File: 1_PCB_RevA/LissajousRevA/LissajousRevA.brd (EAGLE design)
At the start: 100 x 80 mm, 77 parts, among them U101 LM348D, U201 LM348D, U401 LM348D

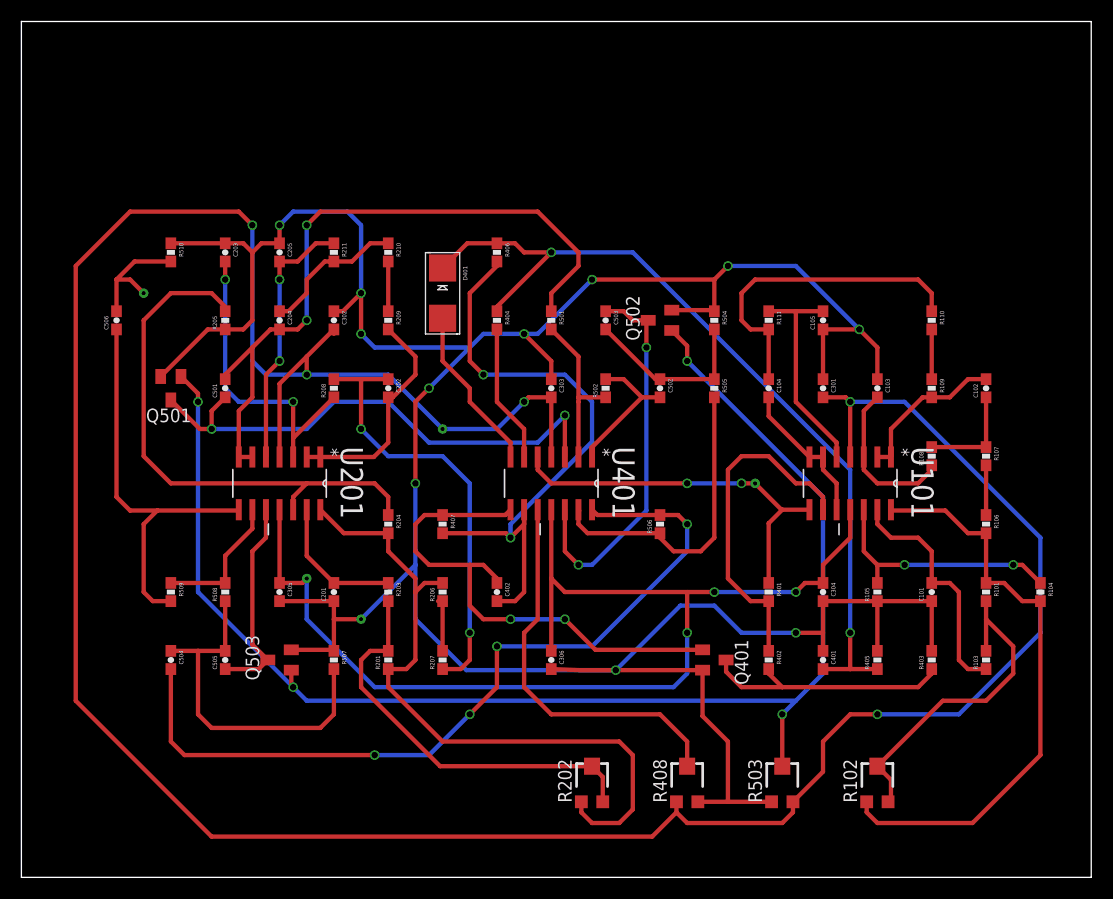
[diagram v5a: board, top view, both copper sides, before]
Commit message: bring test points to bottom of pcb
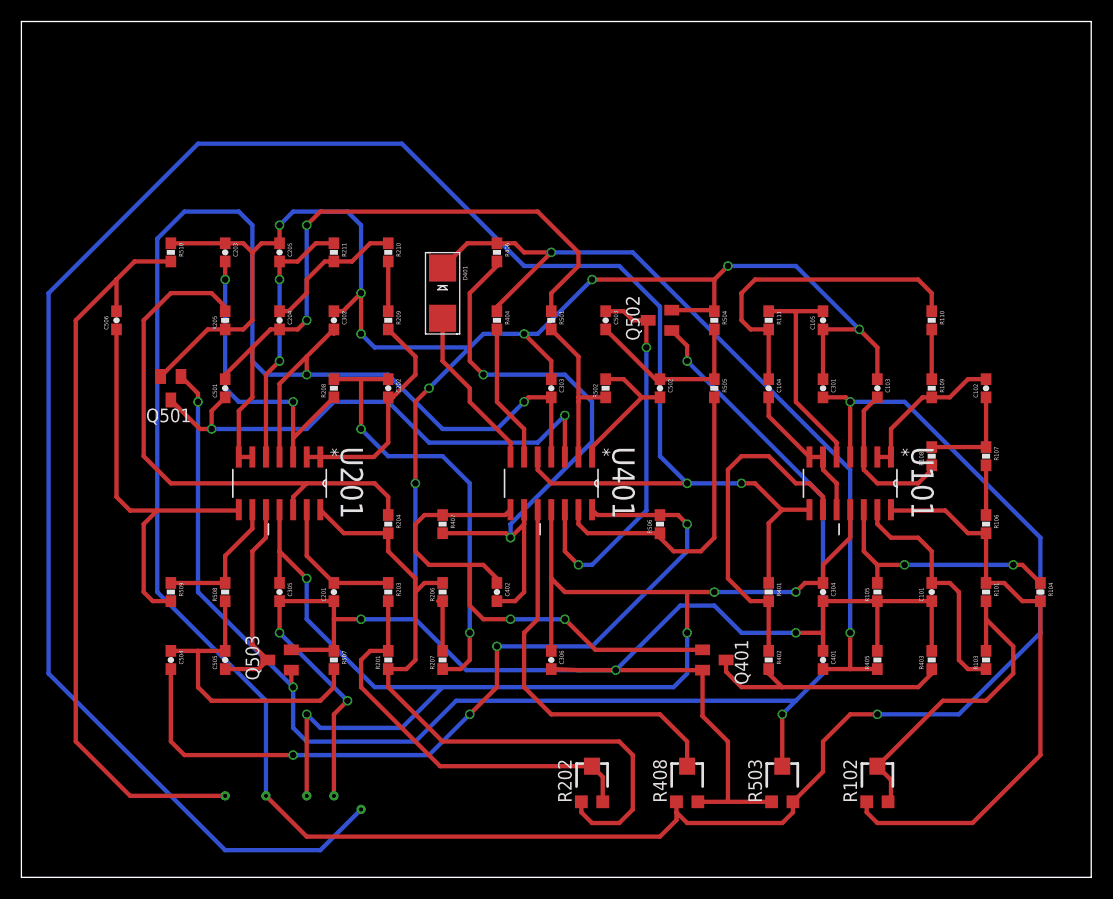
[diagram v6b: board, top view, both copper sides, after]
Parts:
- moved TP304 47.8 mm to (31.8, 6.35)
- moved TP305 47.6 mm to (19.1, 7.62)
- moved TP301 38.1 mm to (22.9, 7.62)
- moved TP302 20.3 mm to (26.7, 7.62)
- moved TP303 16.7 mm to (29.2, 7.62)
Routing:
- net VIEW1: track 35.5 -> 195.5 mm
- net VIEW2: track 11.8 -> 69.6 mm
- net V-: track 107.1 -> 130.4 mm, vias 3 -> 5
- net 0V: track 283.1 -> 302.4 mm, vias 11 -> 14
- net V+: track 273.2 -> 259.1 mm, vias 5 -> 4
- net N$38: track 130.9 -> 136.3 mm
- net N$42: track 34.1 -> 29.0 mm

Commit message: added bigger test pads to pcb
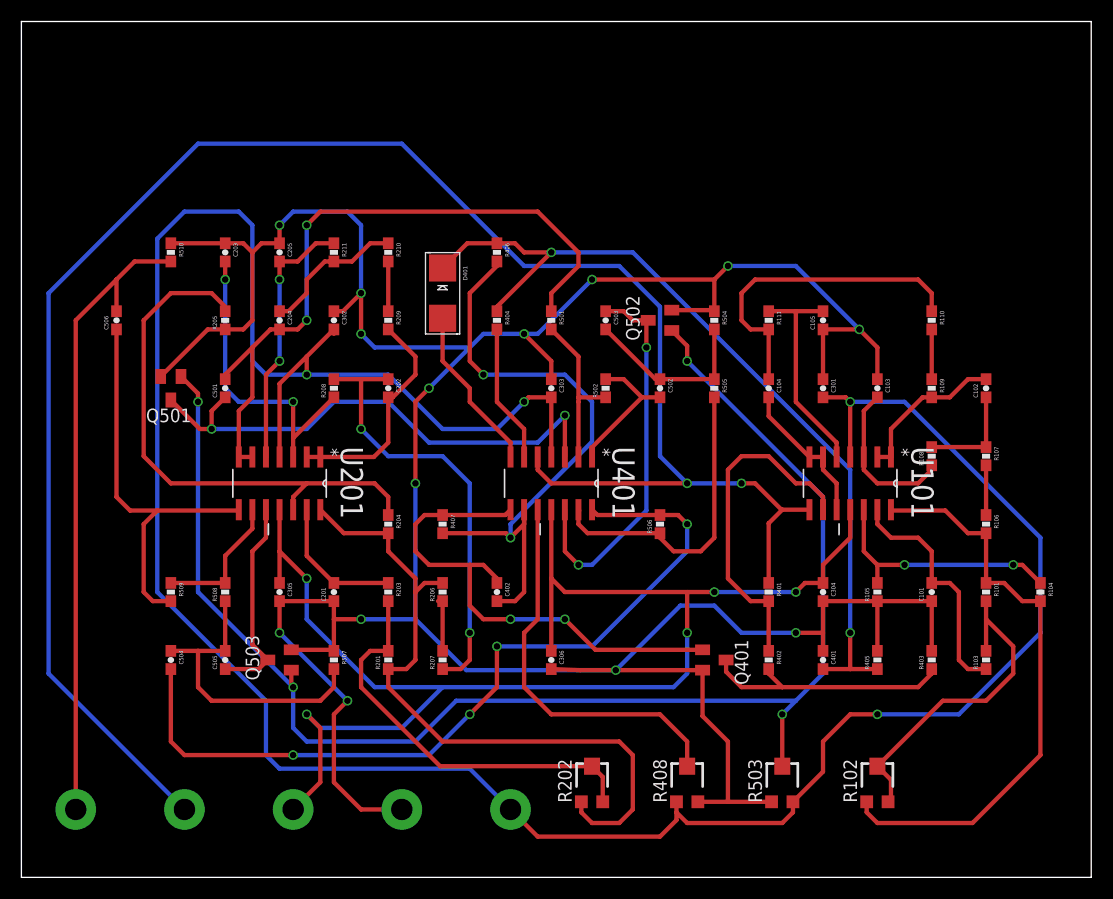
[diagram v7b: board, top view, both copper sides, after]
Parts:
- removed TP304: TEST-POINTTP_15TH_THRU, passives:TP_15TH
- added TO304: PAD, pad:PAD
- TP301, TP302, TP303, TP305: value TEST-POINTTP_15TH_THRU -> PAD; device passives:TP_15TH -> pad:PAD
- moved TP301 22.9 mm to (45.7, 6.35), turned to 0 degrees
- moved TP305 14.0 mm to (5.08, 6.35)
- moved TP303 6.48 mm to (35.6, 6.35)
- moved TP302 1.80 mm to (25.4, 6.35)
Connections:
- net 0V: now also TP303.P$2; no longer TP303.P$1
- net V+: now also TP301.P$2; no longer TP301.P$1
- net V-: now also TP302.P$2; no longer TP302.P$1
- net VIEW1: now also TO304.P$2; no longer TP304.P$1
- net VIEW2: now also TP305.P$2; no longer TP305.P$1
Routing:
- net VIEW1: track 195.5 -> 175.8 mm
- net VIEW2: track 69.6 -> 59.8 mm
- net 0V: track 302.4 -> 308.5 mm
- net V-: track 130.4 -> 133.2 mm
- net V+: track 259.1 -> 256.9 mm
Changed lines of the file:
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@@
 <element name="R206" library="passives" package="0603-RES" value="0R" x="39.37" y="26.67" rot="R90"/>
 <element name="R209" library="passives" package="0603-RES" value="0R" x="34.29" y="52.07" rot="R270"/>
-<element name="TP301" library="passives" package="TP_15TH" value="TEST-POINTTP_15TH_THRU" x="22.86" y="7.62" rot="R90"/>
-<element name="TP303" library="passives" package="TP_15TH" value="TEST-POINTTP_15TH_THRU" x="29.21" y="7.62"/>
 <element name="C301" library="passives" package="0603-CAP" value="100nF" x="74.93" y="45.72" rot="R270"/>
 <element name="C302" library="passives" package="0603-CAP" value="100nF" x="29.21" y="52.07" rot="R270"/>
-<element name="TP302" library="passives" package="TP_15TH" value="TEST-POINTTP_15TH_THRU" x="26.67" y="7.62"/>
 <element name="C303" library="passives" package="0603-CAP" value="100nF" x="49.53" y="45.72" rot="R270"/>
 <element name="C304" library="passives" package="0603-CAP" value="100nF" x="74.93" y="26.67" rot="R270"/>
@@
 <element name="R509" library="passives" package="0603-RES" value="33K" x="13.97" y="26.67" rot="R270"/>
 <element name="R510" library="passives" package="0603-RES" value="33K" x="13.97" y="58.42" rot="R270"/>
-<element name="TP305" library="passives" package="TP_15TH" value="TEST-POINTTP_15TH_THRU" x="19.05" y="7.62"/>
-<element name="TP304" library="passives" package="TP_15TH" value="TEST-POINTTP_15TH_THRU" x="31.75" y="6.35"/>
 <element name="C506" library="passives" package="0603-CAP" value="10nF" x="8.89" y="52.07" rot="R90"/>
+<element name="TP301" library="pad" package="PAD" value="PAD" x="45.72" y="6.35"/>
+<element name="TP302" library="pad" package="PAD" value="PAD" x="25.4" y="6.35"/>
+<element name="TP303" library="pad" package="PAD" value="PAD" x="35.56" y="6.35"/>
+<element name="TO304" library="pad" package="PAD" value="PAD" x="15.24" y="6.35"/>
+<element name="TP305" library="pad" package="PAD" value="PAD" x="5.08" y="6.35"/>
 </elements>
 <signals>
@@
 <contactref element="U101" pad="11"/>
 <contactref element="U201" pad="11"/>
-<contactref element="TP302" pad="P$1"/>
 <contactref element="C304" pad="1"/>
 <contactref element="C306" pad="1"/>
@@
 <via x="26.67" y="27.94" extent="1-16" drill="0.6"/>
 <wire x1="26.67" y1="27.94" x2="24.13" y2="30.48" width="0.4064" layer="1"/>
-<wire x1="26.67" y1="7.62" x2="26.67" y2="15.24" width="0.4064" layer="1"/>
 <via x="26.67" y="15.24" extent="1-16" drill="0.6"/>
 <wire x1="26.67" y1="15.24" x2="27.94" y2="13.97" width="0.4064" layer="16"/>
 <wire x1="27.94" y1="13.97" x2="35.56" y2="13.97" width="0.4064" layer="16"/>
 <wire x1="35.56" y1="13.97" x2="39.37" y2="17.78" width="0.4064" layer="16"/>
+<contactref element="TP302" pad="P$2"/>
+<wire x1="27.94" y1="8.89" x2="27.94" y2="13.97" width="0.4064" layer="1"/>
+<wire x1="27.94" y1="13.97" x2="26.67" y2="15.24" width="0.4064" layer="1"/>
+<wire x1="27.94" y1="8.89" x2="25.4" y2="6.35" width="0.4064" layer="1"/>
 </signal>
 <signal name="V+">
 <contactref element="U101" pad="4"/>
 <contactref element="U201" pad="4"/>
-<contactref element="TP301" pad="P$1"/>
 <contactref element="C303" pad="2"/>
 <contactref element="C302" pad="2"/>
@@
 <wire x1="12.7" y1="59.69" x2="12.7" y2="26.67" width="0.4064" layer="16"/>
 <wire x1="12.7" y1="26.67" x2="22.86" y2="16.51" width="0.4064" layer="16"/>
-<wire x1="22.86" y1="16.51" x2="22.86" y2="7.62" width="0.4064" layer="16"/>
 <wire x1="61.23" y1="6.08" x2="61.23" y2="5.35" width="0.4064" layer="1"/>
 <wire x1="61.23" y1="5.35" x2="59.69" y2="3.81" width="0.4064" layer="1"/>
-<wire x1="59.69" y1="3.81" x2="26.67" y2="3.81" width="0.4064" layer="1"/>
-<wire x1="26.67" y1="3.81" x2="22.86" y2="7.62" width="0.4064" layer="1"/>
+<contactref element="TP301" pad="P$2"/>
+<wire x1="22.86" y1="16.51" x2="22.86" y2="11.43" width="0.4064" layer="16"/>
+<wire x1="22.86" y1="11.43" x2="24.13" y2="10.16" width="0.4064" layer="16"/>
+<wire x1="24.13" y1="10.16" x2="41.91" y2="10.16" width="0.4064" layer="16"/>
+<wire x1="41.91" y1="10.16" x2="45.72" y2="6.35" width="0.4064" layer="16"/>
+<wire x1="59.69" y1="3.81" x2="48.26" y2="3.81" width="0.4064" layer="1"/>
+<wire x1="48.26" y1="3.81" x2="45.72" y2="6.35" width="0.4064" layer="1"/>
 </signal>
 <signal name="0V">
@@
 <contactref element="R205" pad="1"/>
 <contactref element="C201" pad="1"/>
-<contactref element="TP303" pad="P$1"/>
 <contactref element="C301" pad="1"/>
 <contactref element="C302" pad="1"/>
@@
 <via x="31.75" y="24.13" extent="1-16" drill="0.6"/>
 <wire x1="31.75" y1="24.13" x2="29.21" y2="24.13" width="0.4064" layer="1"/>
-<wire x1="29.21" y1="7.62" x2="29.21" y2="15.24" width="0.4064" layer="1"/>
 <wire x1="29.21" y1="15.24" x2="30.48" y2="16.51" width="0.4064" layer="1"/>
 <via x="30.48" y="16.51" extent="1-16" drill="0.6"/>
@@
 <via x="24.13" y="22.86" extent="1-16" drill="0.6"/>
 <wire x1="24.13" y1="22.86" x2="24.13" y2="25.82" width="0.4064" layer="1"/>
+<contactref element="TP303" pad="P$2"/>
+<wire x1="29.21" y1="15.24" x2="29.21" y2="8.89" width="0.4064" layer="1"/>
+<wire x1="29.21" y1="8.89" x2="31.75" y2="6.35" width="0.4064" layer="1"/>
+<wire x1="31.75" y1="6.35" x2="35.56" y2="6.35" width="0.4064" layer="1"/>
 </signal>
 <signal name="N$8">
@@
 <contactref element="R401" pad="1"/>
 <contactref element="U401" pad="5"/>
-<contactref element="TP304" pad="P$1"/>
 <wire x1="48.26" y1="39.2938" x2="48.26" y2="38.1" width="0.4064" layer="1"/>
 <wire x1="48.26" y1="38.1" x2="49.53" y2="36.83" width="0.4064" layer="1"/>
@@
 <wire x1="71.0438" y1="34.3662" x2="68.58" y2="36.83" width="0.4064" layer="1"/>
 <wire x1="68.58" y1="36.83" x2="67.31" y2="36.83" width="0.4064" layer="1"/>
-<wire x1="31.75" y1="6.35" x2="27.94" y2="2.54" width="0.4064" layer="16"/>
-<wire x1="27.94" y1="2.54" x2="19.05" y2="2.54" width="0.4064" layer="16"/>
-<wire x1="19.05" y1="2.54" x2="2.54" y2="19.05" width="0.4064" layer="16"/>
 <wire x1="2.54" y1="19.05" x2="2.54" y2="54.61" width="0.4064" layer="16"/>
 <wire x1="2.54" y1="54.61" x2="16.51" y2="68.58" width="0.4064" layer="16"/>
@@
 <wire x1="59.69" y1="53.34" x2="59.69" y2="39.37" width="0.4064" layer="16"/>
 <wire x1="59.69" y1="39.37" x2="62.23" y2="36.83" width="0.4064" layer="16"/>
+<contactref element="TO304" pad="P$2"/>
+<wire x1="15.24" y1="6.35" x2="2.54" y2="19.05" width="0.4064" layer="16"/>
 </signal>
 <signal name="SINEGEN1">
@@
 <signal name="VIEW2">
 <contactref element="R510" pad="2"/>
-<contactref element="TP305" pad="P$1"/>
 <contactref element="C506" pad="2"/>
 <wire x1="13.97" y1="57.57" x2="10.58" y2="57.57" width="0.4064" layer="1"/>
 <wire x1="10.58" y1="57.57" x2="8.89" y2="55.88" width="0.4064" layer="1"/>
 <wire x1="8.89" y1="55.88" x2="8.89" y2="52.92" width="0.4064" layer="1"/>
-<wire x1="19.05" y1="7.62" x2="10.16" y2="7.62" width="0.4064" layer="1"/>
-<wire x1="10.16" y1="7.62" x2="5.08" y2="12.7" width="0.4064" layer="1"/>
-<wire x1="5.08" y1="12.7" x2="5.08" y2="52.07" width="0.4064" layer="1"/>
+<wire x1="5.08" y1="6.35" x2="5.08" y2="52.07" width="0.4064" layer="1"/>
 <wire x1="5.08" y1="52.07" x2="8.89" y2="55.88" width="0.4064" layer="1"/>
+<contactref element="TP305" pad="P$2"/>
 </signal>
 <signal name="N$38">

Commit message: begin to opt power rail
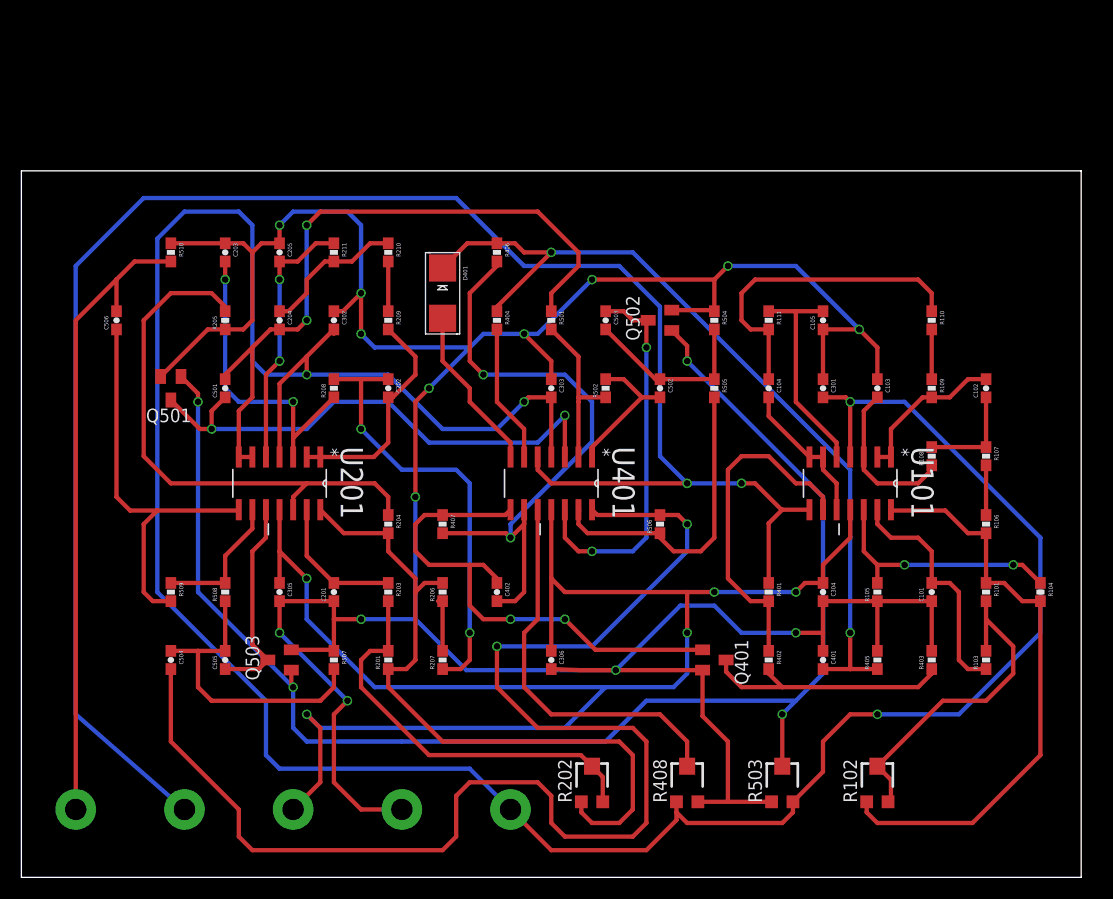
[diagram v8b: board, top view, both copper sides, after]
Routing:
- net N$39: track 77.7 -> 126.9 mm, vias 4 -> 2
- net V-: track 133.2 -> 148.5 mm
- net VIEW1: track 175.8 -> 169.9 mm
- net V+: track 256.9 -> 257.9 mm
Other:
- board size 100 x 80 mm -> 99.1 x 66 mm
